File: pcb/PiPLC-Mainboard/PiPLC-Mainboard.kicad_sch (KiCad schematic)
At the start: 154 parts, among them J1 WJ2EDGRC-5.08-4P, J10 WJ2EDGRC-5.08-4P, J11 WJ2EDGRC-5.08-4P, J12 WJ2EDGRC-5.08-4P, J17 Conn_02x12_Odd_Even, J2 WJ2EDGRC-5.08-4P, J3 WJ2EDGRC-5.08-4P, J4 WJ2EDGRC-5.08-4P, J5 WJ2EDGRC-5.08-4P, J6 WJ2EDGRC-5.08-4P, J7 WJ2EDGRC-5.08-4P, J8 WJ2EDGRC-5.08-4P, J9 WJ2EDGRC-5.08-4P, J99 Rpi GPIO, K1 G5RL-1A-E-TV8 DC24, K2 G5RL-1A-E-TV8 DC24, K3 G5RL-1A-E-TV8 DC24, K4 G5RL-1A-E-TV8 DC24, K5 G5RL-1A-E-TV8 DC24, K6 G5RL-1A-E-TV8 DC24, K7 G5RL-1A-E-TV8 DC24, K8 G5RL-1A-E-TV8 DC24, Q1 AO3400A, Q2 AO3400A, Q3 AO3400A, Q4 AO3400A, Q5 AO3400A, Q6 AO3400A, Q7 AO3400A, Q8 AO3400A, Q9 SS8550 Y2, U1 TPS54331D, U10 EL817C, U11 EL817C, U12 ISO3082DWR, U2 NCN5121, U3 ISO1540, U4 EL817C, U5 EL817C, U6 EL817C, U7 EL817C, U8 EL817C, U9 EL817C, Y2 16MHz

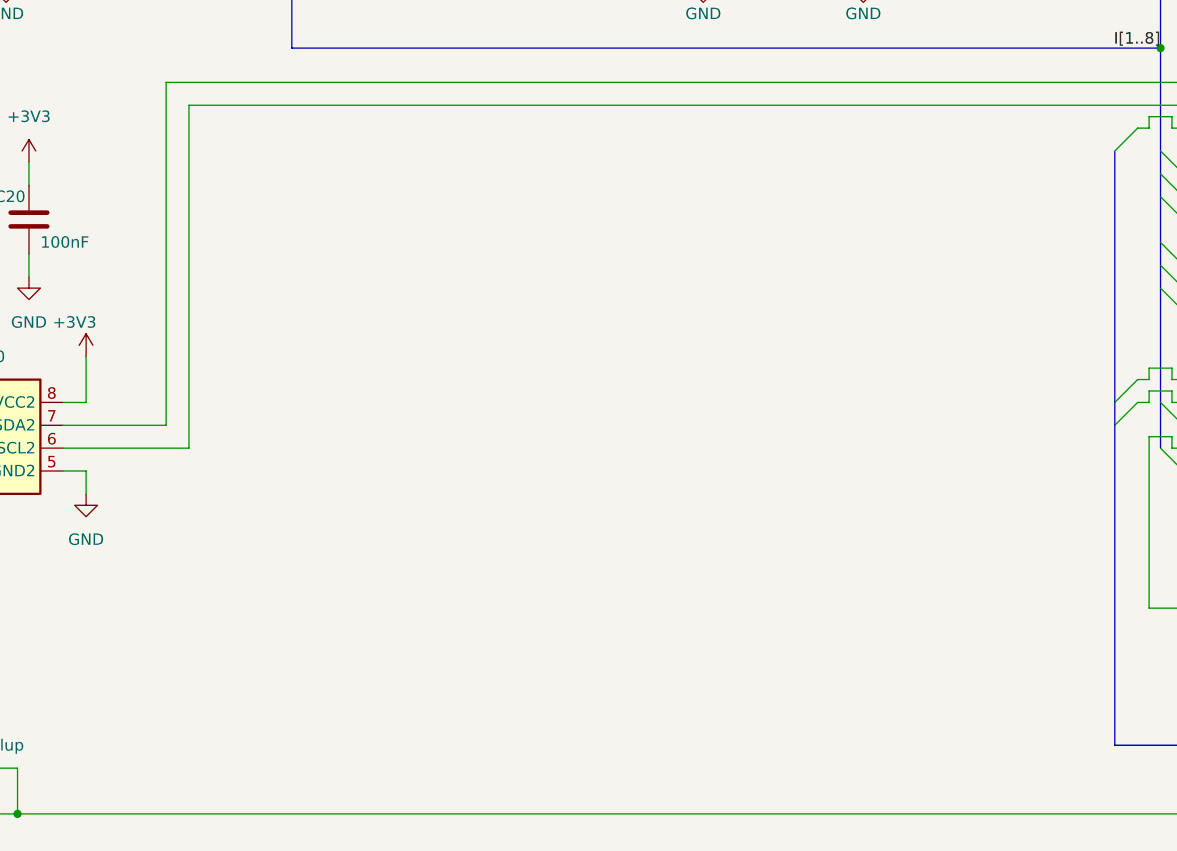
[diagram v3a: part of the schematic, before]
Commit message: [Mainboard] Add PCF8523 realtime clock
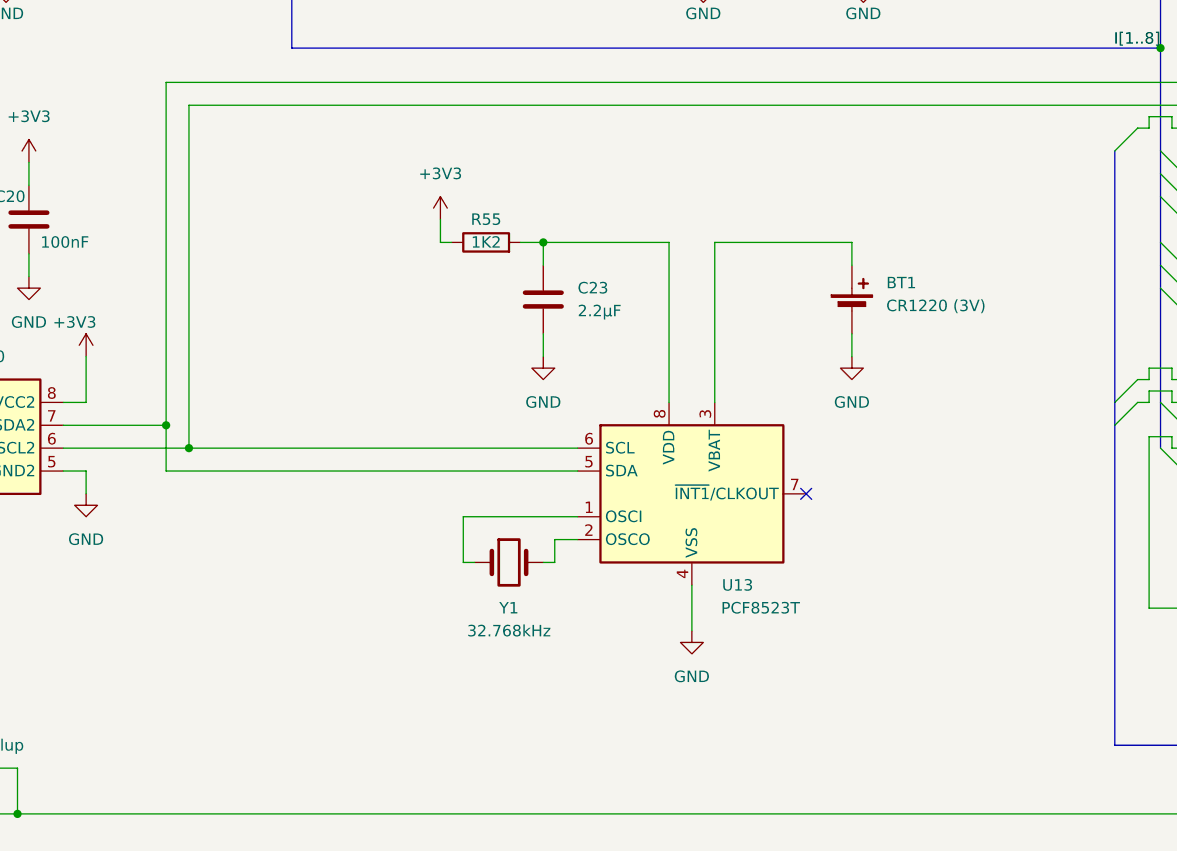
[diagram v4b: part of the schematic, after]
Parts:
- added BT1: CR1220 (3V), MeineBib:CR1220_Holder, symbol Device:Battery_Cell
- added C23: 2.2µF, Capacitor_SMD:C_0603_1608Metric, symbol Device:C
- added R55: 1K2, Resistor_SMD:R_0603_1608Metric, symbol Device:R
- added U13: PCF8523T, Package_SO:SOIC-8_3.9x4.9mm_P1.27mm, symbol Timer_RTC:PCF8523T
- added Y1: 32.768kHz, Crystal:Crystal_SMD_3215-2Pin_3.2x1.5mm, symbol Device:Crystal
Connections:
- net +3V3: now also R55.1
- net GND: now also BT1.2 (-), C23.2, U13.4 (VSS)
- net I²C SCL: now also U13.6 (SCL)
- net I²C SDA: now also U13.5 (SDA)
- new net: C23.1, R55.2, U13.8 (VDD)
- new net: U13.1 (OSCI), Y1.1
- new net: U13.2 (OSCO), Y1.2
- new net: BT1.1 (+), U13.3 (VBAT)
- no-connect marks 66 -> 67

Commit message: [Mainboard] Add ground connector to Relay footprint for addon board
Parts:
- K1, K2, K3, K4, K5, K6, K7, K8: footprint Relay_THT:Relay_SPST_Omron_G2RL-1A-E -> MeineBib:Relay_SPST_Omron_G2RL-1A-E_GroundMod; symbol Relay:G2RL-1A-E -> MeineBib:Relay_SPST-NO_GndMod
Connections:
- net GND: now also K1.GND, K2.GND, K3.GND, K4.GND, K5.GND, K6.GND, K7.GND, K8.GND

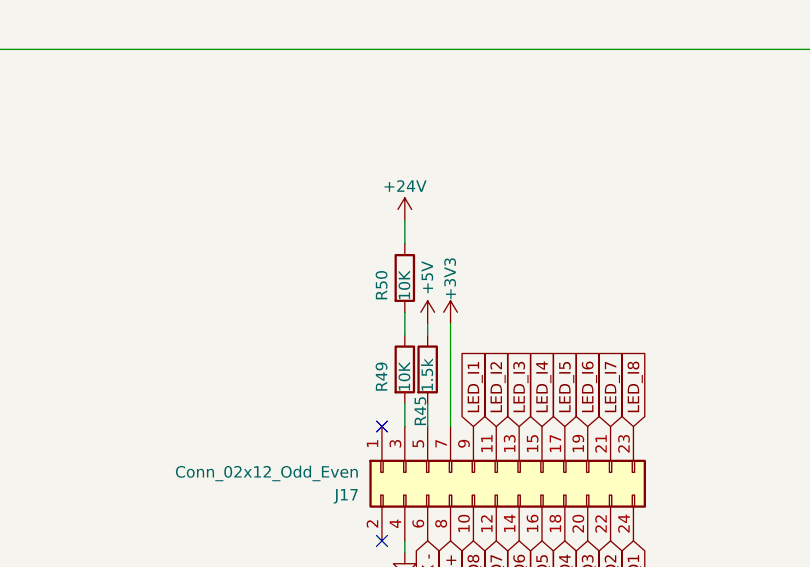
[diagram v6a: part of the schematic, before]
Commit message: PENDING VALIDATION - Update to new KiCAD version - update current limit resistors to not burn my eyes out
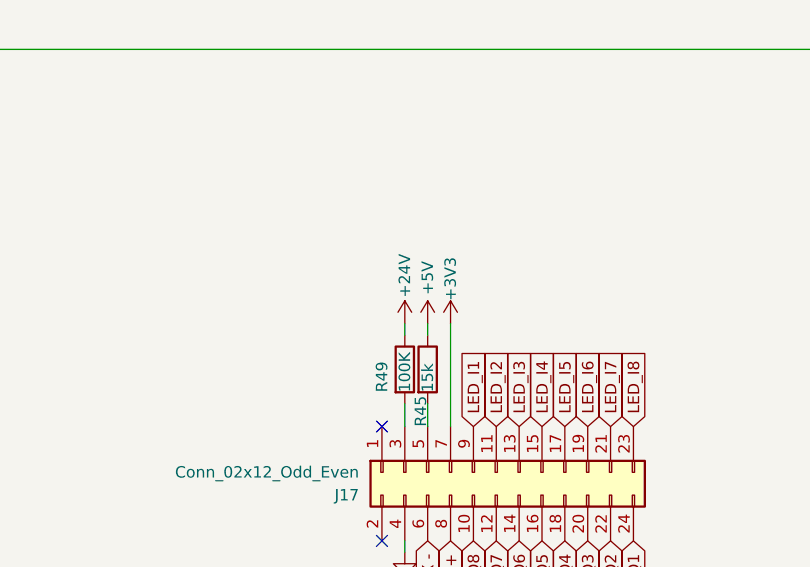
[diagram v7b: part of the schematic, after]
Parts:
- removed R50: 10K, Resistor_SMD:R_0603_1608Metric, symbol Device:R
- R45: value 1.5k -> 15k; LCSC C22843 -> C22809
- R49: value 10K -> 100K; LCSC C25804 -> C25803
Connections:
- net +24V: now also R49.1
